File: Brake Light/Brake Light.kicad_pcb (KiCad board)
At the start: 2 copper layers, 96.5 x 25.4 mm, 45 parts, among them J1 CONN_01X04

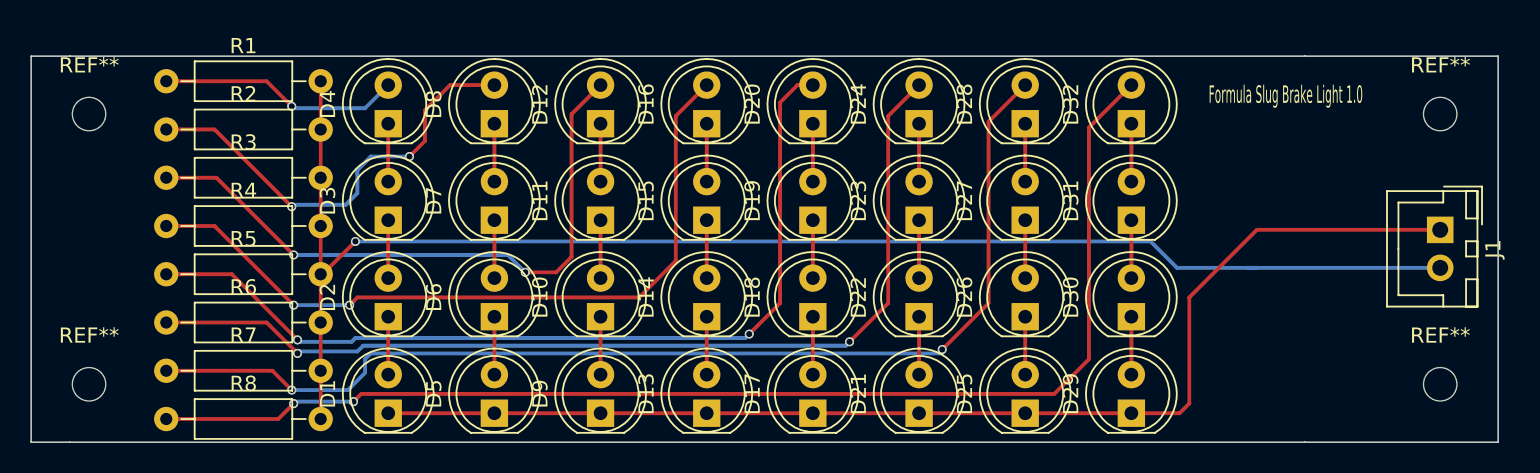
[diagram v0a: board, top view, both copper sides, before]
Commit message: Cleaned up tracks
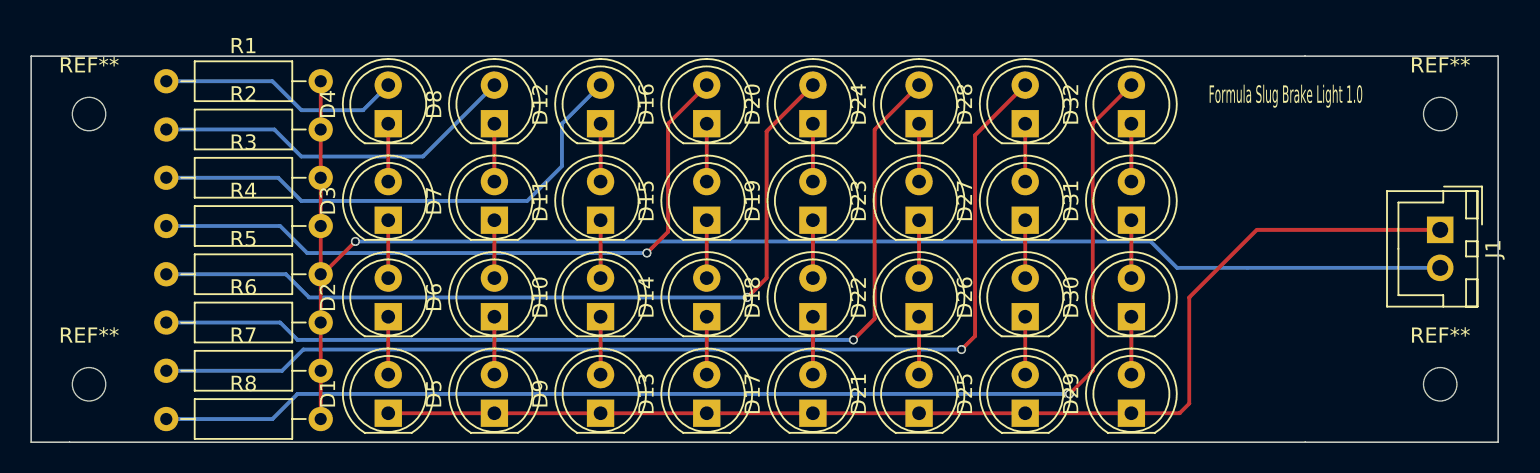
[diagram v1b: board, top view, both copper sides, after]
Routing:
- net Net-(D12-Pad2): track 41.8 -> 34.0 mm, vias 2 -> 0
- net Net-(D20-Pad2): track 59.1 -> 54.6 mm, vias 2 -> 1
- net Net-(D8-Pad2): track 29.1 -> 24.7 mm, vias 2 -> 0
- net Net-(D16-Pad2): track 49.3 -> 45.0 mm, vias 2 -> 1
- net Net-(D28-Pad2): track 73.0 -> 72.0 mm, vias 2 -> 1
- net Net-(D24-Pad2): track 64.9 -> 64.2 mm, vias 2 -> 1
- net GND: track 98.1 -> 97.5 mm
- net Net-(D32-Pad2): track 81.5 -> 82.1 mm, vias 2 -> 1
- net Net-(D4-Pad2): track 16.0 -> 16.1 mm, vias 1 -> 0

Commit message: centered LEDs
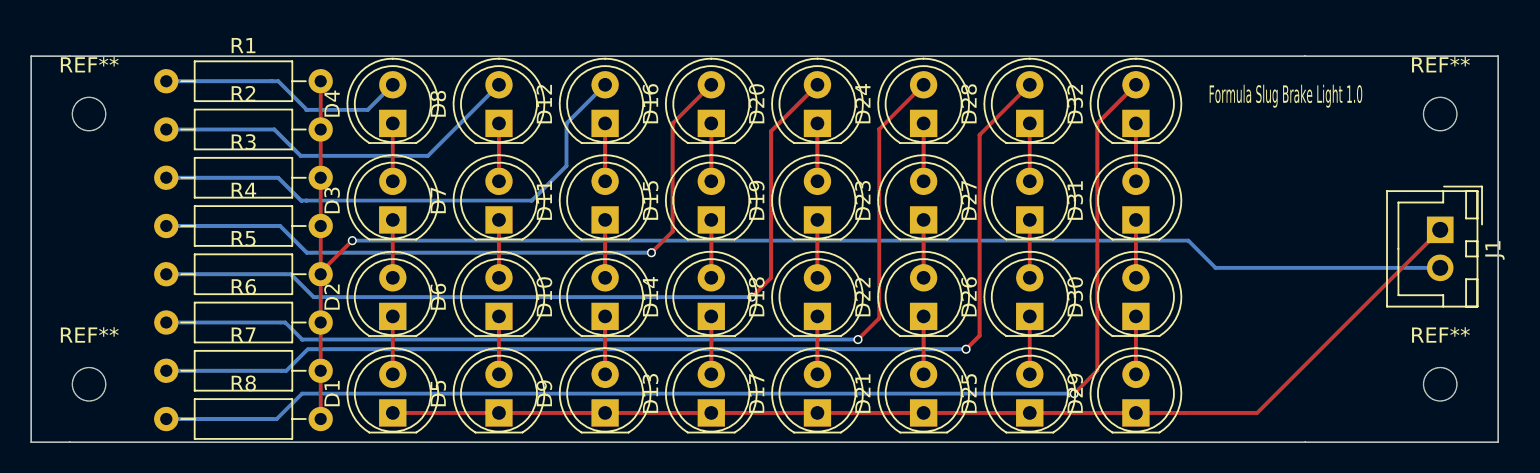
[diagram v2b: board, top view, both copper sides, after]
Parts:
- moved D13 0.30 mm to (141.3, 81.9)
- moved D15 0.30 mm to (141.3, 69.2)
- moved D21 0.30 mm to (155.2, 81.9)
- moved D23 0.30 mm to (155.2, 69.2)
- moved D29 0.30 mm to (169.2, 81.9)
- moved D31 0.30 mm to (169.2, 69.2)
- moved D16 0.30 mm to (141.3, 62.8)
- moved D24 0.30 mm to (155.2, 62.8)
- moved D32 0.30 mm to (169.2, 62.8)
- moved D14 0.30 mm to (141.3, 75.5)
- moved D22 0.30 mm to (155.2, 75.5)
- moved D30 0.30 mm to (169.2, 75.5)
- moved D1 0.30 mm to (120.3, 81.9)
- moved D3 0.30 mm to (120.3, 69.2)
- moved D5 0.30 mm to (127.3, 81.9)
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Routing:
- net +12V: track 78.3 -> 73.9 mm
